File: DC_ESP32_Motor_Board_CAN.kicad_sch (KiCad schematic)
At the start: 32 parts, among them IC1 VNH7100BASTR, IC2 TJA1050T_CM, J1 SM04B-SRSS-TB, J2 SM04B-SRSS-TB, J3 XT30PB, J4 XT30PB, J5 Conn_01x03_Pin, J6 Conn_01x02_Pin, J7 XT30PB, SW1 DSHP04TJGER, U1 MOUDLE-SEEEDUINO-XIAO-ESP32C3

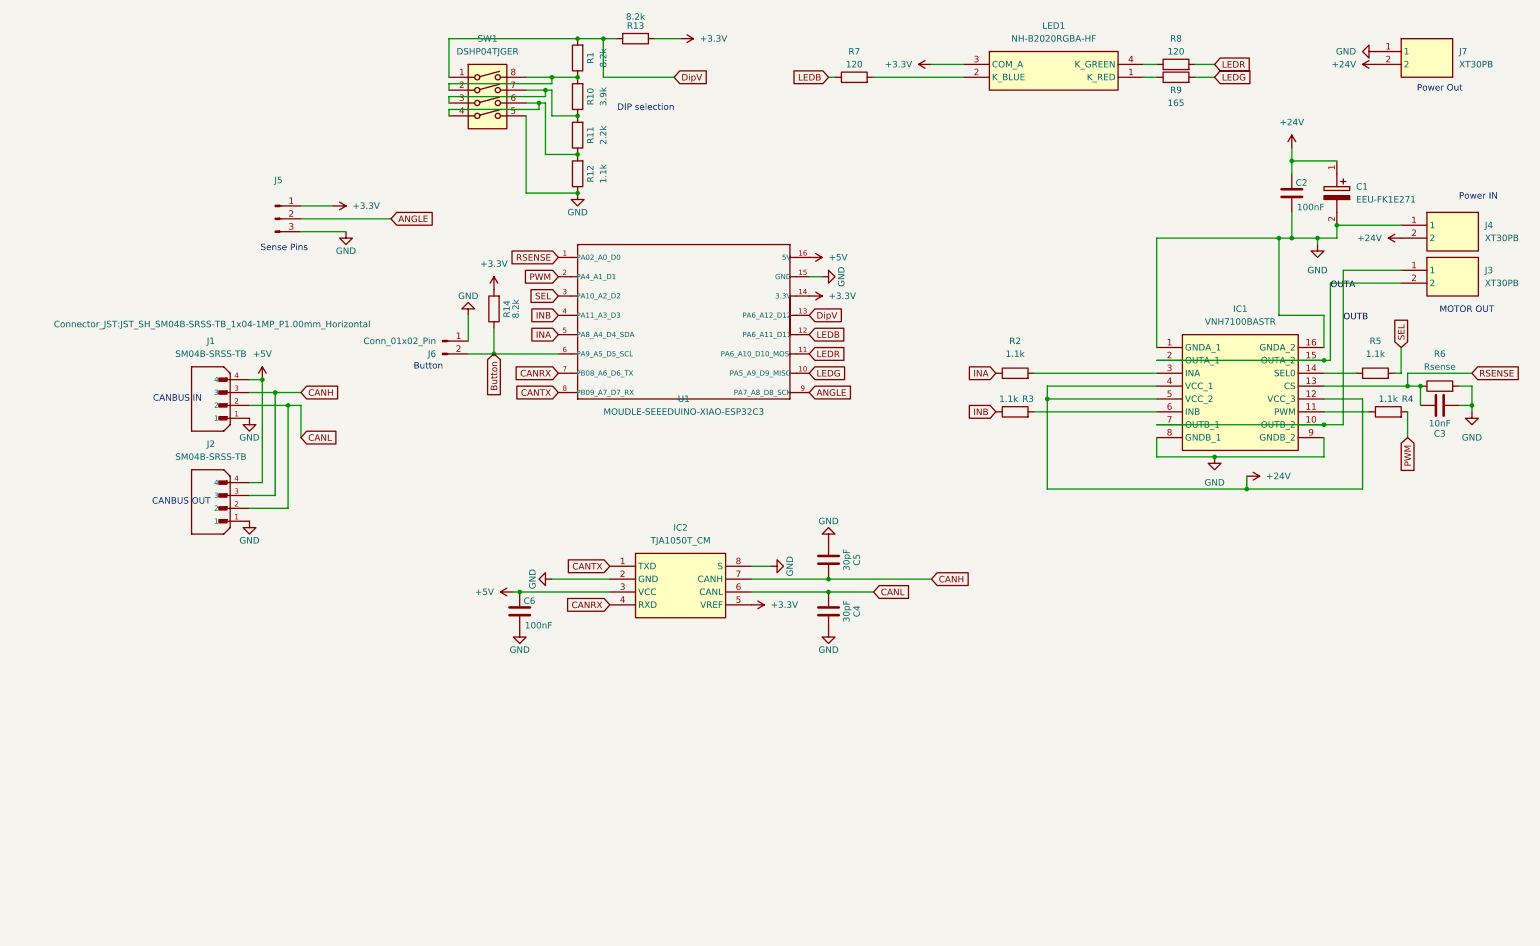
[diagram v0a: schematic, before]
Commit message: Update with mounting holes
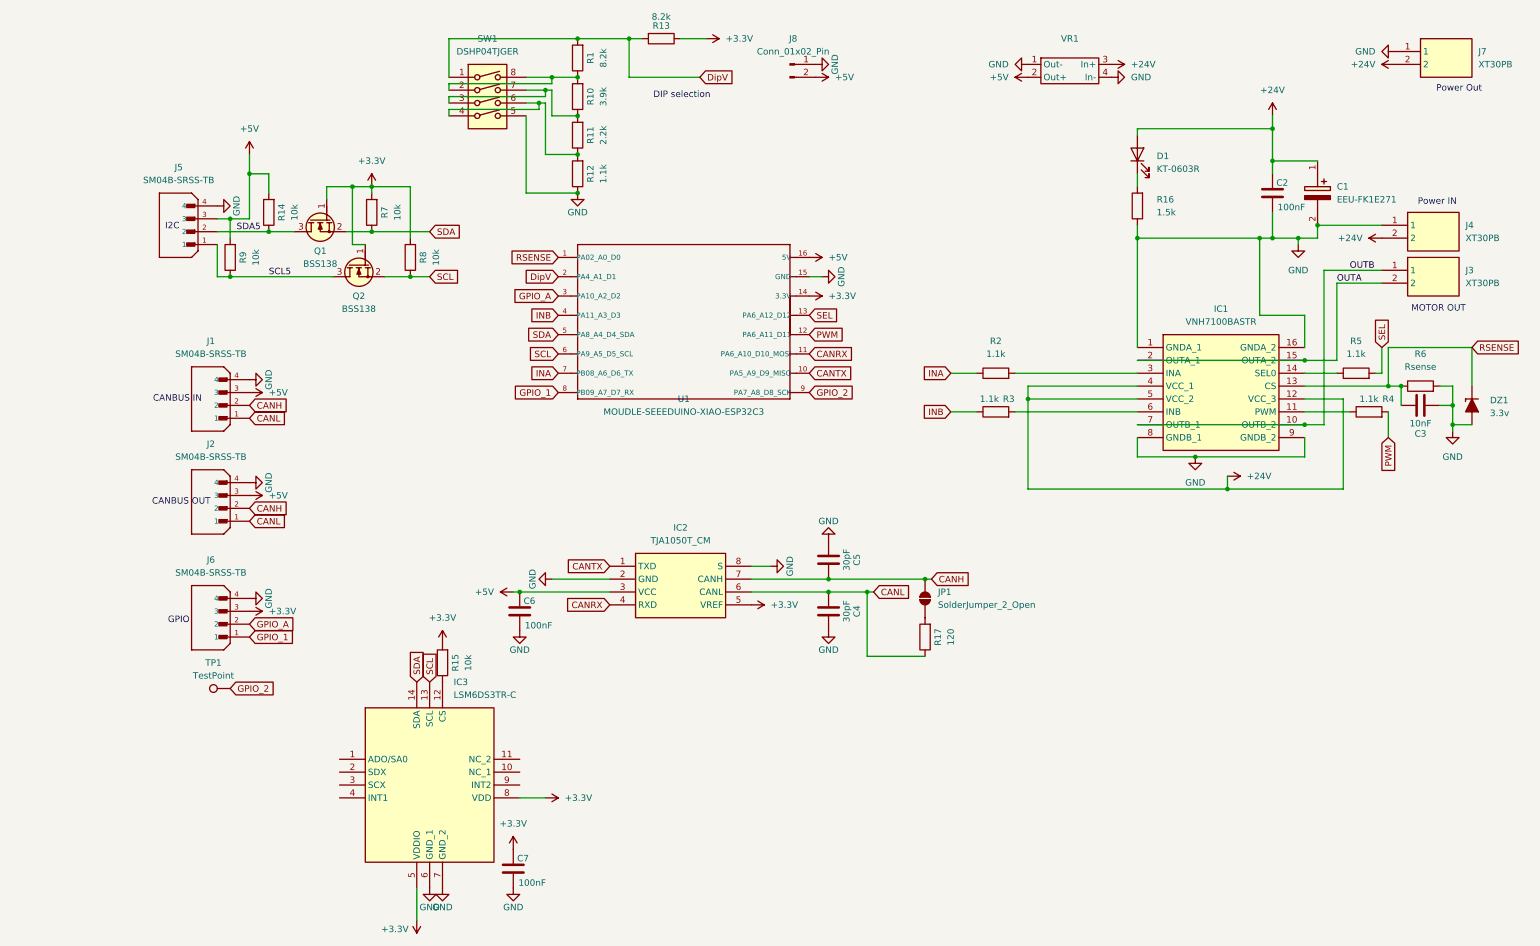
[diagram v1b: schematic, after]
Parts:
- removed J5: Conn_01x03_Pin, Connector_JST:JST_SH_SM03B-SRSS-TB_1x03-1MP_P1.00mm_Horizontal, symbol Connector:Conn_01x03_Pin
- removed J6: Conn_01x02_Pin, Connector_JST:JST_SH_BM02B-SRSS-TB_1x02-1MP_P1.00mm_Vertical, symbol Connector:Conn_01x02_Pin
- removed LED1: NH-B2020RGBA-HF, SamacSys_Parts:NHB2020RGBAHF, symbol SamacSys_Parts:NH-B2020RGBA-HF
- added C7: 100nF, Capacitor_SMD:C_0805_2012Metric, symbol Device:C
- added D1: KT-0603R, LED_SMD:LED_0603_1608Metric, symbol Device:LED
- added DZ1: 3.3v, Diode_SMD:D_SOD-123, symbol PCM_Diode_Zener_AKL:D_Zener_Generic
- added IC3: LSM6DS3TR-C, LSM6DS3USTR, symbol SamacSys_Parts:LSM6DS3TR-C
- added J5, J6: SM04B-SRSS-TB, Connector_JST:JST_SH_SM04B-SRSS-TB_1x04-1MP_P1.00mm_Horizontal, symbol SamacSys_Parts:B4B-XH-A_LF__SN_
- added J8: Conn_01x02_Pin, Connector_PinHeader_1.00mm:PinHeader_1x02_P1.00mm_Vertical, symbol Connector:Conn_01x02_Pin
- added JP1: SolderJumper_2_Open, Jumper:SolderJumper-2_P1.3mm_Open_RoundedPad1.0x1.5mm, symbol Jumper:SolderJumper_2_Open
- added Q1, Q2: BSS138, PCM_Package_TO_SOT_SMD_AKL:SOT-23, symbol PCM_Transistor_MOSFET_AKL:BSS138
- added R15: 10k, Resistor_SMD:R_0402_1005Metric, symbol Device:R
- added R16: 1.5k, Resistor_SMD:R_0402_1005Metric, symbol Device:R
- added R17: 120, Resistor_SMD:R_0402_1005Metric, symbol Device:R
- added TP1: TestPoint, TestPoint:TestPoint_Pad_1.0x1.0mm, symbol Connector:TestPoint
- added VR1: ~, Library:EY9 reg board, symbol Personal:Reg_Board
- J3, J4: footprint JST_Sorted:xt30_Right_Angle -> Library:Xt30 Horizontal
- R14: value 8.2k -> 10k
- R6: footprint Resistor_THT:R_Axial_DIN0204_L3.6mm_D1.6mm_P5.08mm_Horizontal -> Resistor_THT:R_Axial_DIN0204_L3.6mm_D1.6mm_P2.54mm_Vertical
- R7, R8: value 120 -> 10k
- R9: value 165 -> 10k
- SW1: footprint Button_Switch_SMD:SW_DIP_SPSTx04_Slide_KingTek_DSHP04TJ_W5.25mm_P1.27mm_JPin -> Button_Switch_SMD:SW_DIP_SPSTx04_Slide_Copal_CHS-04A_W5.08mm_P1.27mm_JPin
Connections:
- net +24V: now also D1.2 (A), VR1.3 (In+)
- net +3.3V: now also R7.2, R8.2, C7.1, IC3.5 (VDDIO), IC3.8 (VDD), J6.3, Q1.1 (G), Q2.1 (G), R15.2; no longer R14.2
- net +5V: now also J1.3, J2.3, R14.2, R9.2, J5.3, J8.2 (Pin_2), VR1.2 (Out+); no longer J1.4, J2.4
- net CANH: now also J1.2, J2.2, JP1.2 (B); no longer J1.3, J2.3
- net CANL: now also J1.1, J2.1, R17.1; no longer J1.2, J2.2
- net CANRX: now also U1.11 (PA6_A10_D10_MOSI); no longer U1.7 (PB08_A6_D6_TX)
- net CANTX: now also U1.10 (PA5_A9_D9_MISO); no longer U1.8 (PB09_A7_D7_RX)
- net DipV: now also U1.2 (PA4_A1_D1); no longer U1.13 (PA6_A12_D12)
- net GND: now also J1.4, J2.4, C7.2, DZ1.2 (A), IC3.6 (GND_1), IC3.7 (GND_2), J5.4, J6.4, J8.1 (Pin_1), R16.1, VR1.1 (Out-), VR1.4 (In-); no longer J1.1, J2.1
- net INA: now also U1.7 (PB08_A6_D6_TX); no longer U1.5 (PA8_A4_D4_SDA)
- net PWM: now also U1.12 (PA6_A11_D11); no longer U1.2 (PA4_A1_D1)
- net RSENSE: now also DZ1.1 (K)
- net SEL: now also U1.13 (PA6_A12_D12); no longer U1.3 (PA10_A2_D2)
- net SCL5: now reaches R9.1
- net SCL5: now also J5.1, Q2.3 (D)
- net SCL: now reaches R8.1
- net SCL: now also U1.6 (PA9_A5_D5_SCL), IC3.13 (SCL), Q2.2 (S)
- net ANGLE renamed GPIO_2
- net GPIO_2: now also TP1.1
- net Button renamed SDA5
- net SDA5: now also J5.2, Q1.3 (D); no longer U1.6 (PA9_A5_D5_SCL)
- net LEDB renamed SDA
- net SDA: now also U1.5 (PA8_A4_D4_SDA), IC3.14 (SDA), Q1.2 (S); no longer U1.12 (PA6_A11_D11)
- removed net LEDG: R9.2, U1.10 (PA5_A9_D9_MISO)
- removed net LEDR: R8.2, U1.11 (PA6_A10_D10_MOSI)
- new net: JP1.1 (A), R17.2
- new net: IC3.12 (CS), R15.1
- new net: D1.1 (K), R16.2
- new net GPIO_1: J6.1, U1.8 (PB09_A7_D7_RX)
- new net GPIO_A: J6.2, U1.3 (PA10_A2_D2)
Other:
- note added: "GPIO"
- note added: "I2C"
- note removed: "Button"
- note removed: "Sense Pins"
- moved on the sheet: C1, C2, C3, IC1, J3, J4, J7, R13, R2, R3, R4, R5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

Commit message: Last Update to PCBWAY
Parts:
- removed TP1: TestPoint, TestPoint:TestPoint_Pad_1.0x1.0mm, symbol Connector:TestPoint
- added C8: 100nF, Capacitor_SMD:C_0805_2012Metric, symbol Device:C
- C1, J3, J4, J7, R6, U1, VR1: now left out of the parts list
- DZ1: value 3.3v -> MM1Z3V3
- J8: value Conn_01x02_Pin -> Conn_01x03_Pin; footprint Connector_PinHeader_1.00mm:PinHeader_1x02_P1.00mm_Vertical -> Connector_PinHeader_1.00mm:PinHeader_1x03_P1.00mm_Vertical; symbol Connector:Conn_01x02_Pin -> Connector:Conn_01x03_Pin
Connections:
- net +3.3V: now also C8.1
- net GND: now also C8.2
- net GPIO_2: now also J8.3 (Pin_3)
